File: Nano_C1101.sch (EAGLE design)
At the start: 7 parts

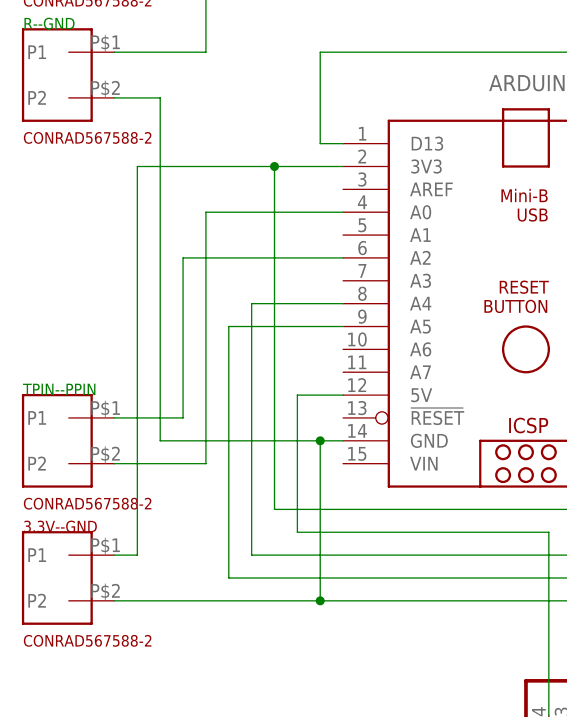
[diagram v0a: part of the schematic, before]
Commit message: few typos, 3V3 -> 5V
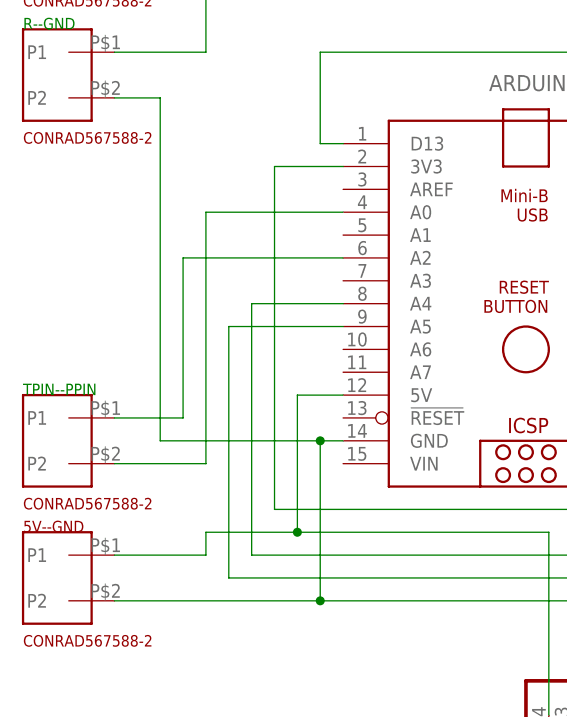
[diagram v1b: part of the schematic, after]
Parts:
- renumbered 3.3V--GND to 5V--GND
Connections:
- net 3V3: no longer 5V--GND.P1
- net 5V: now also 5V--GND.P1
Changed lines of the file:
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@@
 </classes>
 <parts>
-<part name="3.3V--GND" library="johannes" deviceset="CONRAD567588-2" device=""/>
+<part name="5V--GND" library="johannes" deviceset="CONRAD567588-2" device=""/>
 <part name="TPIN--PPIN" library="johannes" deviceset="CONRAD567588-2" device=""/>
 <part name="R--GND" library="johannes" deviceset="CONRAD567588-2" device=""/>
@@
 </plain>
 <instances>
-<instance part="3.3V--GND" gate="G$1" x="-15.24" y="38.1" smashed="yes" rot="R270">
+<instance part="5V--GND" gate="G$1" x="-15.24" y="38.1" smashed="yes" rot="R270">
 <attribute name="VALUE" x="-20.32" y="30.48" size="1.27" layer="94"/>
 <attribute name="NAME" x="-20.32" y="43.18" size="1.27" layer="94"/>
@@
 <wire x1="-5.08" y1="53.34" x2="12.7" y2="53.34" width="0.1524" layer="91"/>
 <junction x="12.7" y="53.34"/>
-<pinref part="3.3V--GND" gate="G$1" pin="P2"/>
+<pinref part="5V--GND" gate="G$1" pin="P2"/>
 <wire x1="-10.16" y1="35.56" x2="12.7" y2="35.56" width="0.1524" layer="91"/>
 <junction x="12.7" y="35.56"/>
@@
 <wire x1="73.66" y1="55.88" x2="86.36" y2="55.88" width="0.1524" layer="91"/>
 <wire x1="7.62" y1="45.72" x2="7.62" y2="83.82" width="0.1524" layer="91"/>
-<wire x1="-7.62" y1="83.82" x2="-7.62" y2="40.64" width="0.1524" layer="91"/>
-<pinref part="3.3V--GND" gate="G$1" pin="P1"/>
-<wire x1="-7.62" y1="40.64" x2="-10.16" y2="40.64" width="0.1524" layer="91"/>
-<wire x1="-7.62" y1="83.82" x2="7.62" y2="83.82" width="0.1524" layer="91"/>
 <pinref part="ARDUINO_NANO1" gate="G$1" pin="3V3"/>
 <wire x1="7.62" y1="83.82" x2="15.24" y2="83.82" width="0.1524" layer="91"/>
-<junction x="7.62" y="83.82"/>
 </segment>
 </net>
@@
 <pinref part="OLED" gate="A" pin="4"/>
 <wire x1="38.1" y1="43.18" x2="38.1" y2="22.86" width="0.1524" layer="91"/>
+<pinref part="5V--GND" gate="G$1" pin="P1"/>
+<wire x1="-10.16" y1="40.64" x2="0" y2="40.64" width="0.1524" layer="91"/>
+<wire x1="0" y1="40.64" x2="0" y2="43.18" width="0.1524" layer="91"/>
+<wire x1="0" y1="43.18" x2="10.16" y2="43.18" width="0.1524" layer="91"/>
+<junction x="10.16" y="43.18"/>
 </segment>
 </net>
@@
 </sheet>
 </sheets>
+<errors>
+</errors>
 </schematic>
 </drawing>

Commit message: Semi-final version of Nano_C1101
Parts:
- added JP1: (no value), adafruit:PINHD-1X1
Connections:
- new net N$1: ARDUINO_NANO1.D6, JP1.1
- net G-RGB: now also ARDUINO_NANO1.D7; no longer ARDUINO_NANO1.D6
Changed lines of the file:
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@@
 <layer number="54" name="bGND_GNDA" color="1" fill="9" visible="no" active="no"/>
 <layer number="56" name="wert" color="7" fill="1" visible="no" active="no"/>
+<layer number="57" name="tCAD" color="7" fill="1" visible="no" active="no"/>
+<layer number="59" name="tCarbon" color="7" fill="1" visible="no" active="no"/>
+<layer number="60" name="bCarbon" color="7" fill="1" visible="no" active="no"/>
 <layer number="88" name="SimResults" color="9" fill="1" visible="yes" active="yes"/>
 <layer number="89" name="SimProbes" color="9" fill="1" visible="yes" active="yes"/>
@@
 <layer number="97" name="Info" color="7" fill="1" visible="yes" active="yes"/>
 <layer number="98" name="Guide" color="6" fill="1" visible="yes" active="yes"/>
+<layer number="99" name="SpiceOrder" color="7" fill="1" visible="no" active="no"/>
 <layer number="100" name="Muster" color="7" fill="1" visible="no" active="no"/>
 <layer number="101" name="Patch_Top" color="12" fill="4" visible="yes" active="yes"/>
@@
 <layer number="106" name="bPlate" color="7" fill="1" visible="yes" active="yes"/>
 <layer number="107" name="Crop" color="7" fill="1" visible="yes" active="yes"/>
+<layer number="108" name="fp8" color="7" fill="1" visible="no" active="yes"/>
+<layer number="109" name="fp9" color="7" fill="1" visible="no" active="yes"/>
+<layer number="110" name="fp0" color="7" fill="1" visible="no" active="yes"/>
+<layer number="111" name="LPC17xx" color="7" fill="1" visible="no" active="yes"/>
+<layer number="112" name="tSilk" color="7" fill="1" visible="no" active="yes"/>
+<layer number="113" name="ReferenceLS" color="7" fill="1" visible="no" active="no"/>
 <layer number="116" name="Patch_BOT" color="9" fill="4" visible="yes" active="yes"/>
+<layer number="118" name="Rect_Pads" color="7" fill="1" visible="no" active="no"/>
 <layer number="121" name="_tsilk" color="7" fill="1" visible="yes" active="yes"/>
 <layer number="122" name="_bsilk" color="7" fill="1" visible="yes" active="yes"/>
+<layer number="123" name="tTestmark" color="7" fill="1" visible="no" active="yes"/>
+<layer number="124" name="bTestmark" color="7" fill="1" visible="no" active="yes"/>
 <layer number="125" name="_tNames" color="7" fill="1" visible="yes" active="yes"/>
+<layer number="126" name="_bNames" color="7" fill="1" visible="no" active="yes"/>
+<layer number="127" name="_tValues" color="7" fill="1" visible="no" active="yes"/>
+<layer number="128" name="_bValues" color="7" fill="1" visible="no" active="yes"/>
+<layer number="129" name="Mask" color="7" fill="1" visible="yes" active="yes"/>
+<layer number="131" name="tAdjust" color="7" fill="1" visible="no" active="yes"/>
+<layer number="132" name="bAdjust" color="7" fill="1" visible="no" active="yes"/>
 <layer number="144" name="Drill_legend" color="7" fill="1" visible="yes" active="yes"/>
+<layer number="150" name="Notes" color="7" fill="1" visible="no" active="yes"/>
 <layer number="151" name="HeatSink" color="7" fill="1" visible="yes" active="yes"/>
+<layer number="152" name="_bDocu" color="7" fill="1" visible="no" active="yes"/>
+<layer number="153" name="FabDoc1" color="6" fill="1" visible="no" active="no"/>
+<layer number="154" name="FabDoc2" color="2" fill="1" visible="no" active="no"/>
+<layer number="155" name="FabDoc3" color="7" fill="15" visible="no" active="no"/>
+<layer number="199" name="Contour" color="7" fill="1" visible="no" active="yes"/>
 <layer number="200" name="200bmp" color="1" fill="10" visible="yes" active="yes"/>
 <layer number="201" name="201bmp" color="2" fill="10" visible="yes" active="yes"/>
@@
 <layer number="223" name="223bmp" color="24" fill="1" visible="no" active="no"/>
 <layer number="224" name="224bmp" color="25" fill="1" visible="no" active="no"/>
+<layer number="225" name="225bmp" color="7" fill="1" visible="yes" active="yes"/>
+<layer number="226" name="226bmp" color="7" fill="1" visible="yes" active="yes"/>
+<layer number="227" name="227bmp" color="7" fill="1" visible="yes" active="yes"/>
+<layer number="228" name="228bmp" color="7" fill="1" visible="yes" active="yes"/>
+<layer number="229" name="229bmp" color="7" fill="1" visible="yes" active="yes"/>
+<layer number="230" name="230bmp" color="7" fill="1" visible="yes" active="yes"/>
+<layer number="231" name="Eagle3D_PG1" color="7" fill="1" visible="no" active="no"/>
+<layer number="232" name="Eagle3D_PG2" color="7" fill="1" visible="no" active="no"/>
+<layer number="233" name="Eagle3D_PG3" color="7" fill="1" visible="no" active="no"/>
+<layer number="248" name="Housing" color="7" fill="1" visible="no" active="yes"/>
+<layer number="249" name="Edge" color="7" fill="1" visible="no" active="yes"/>
 <layer number="250" name="Descript" color="3" fill="1" visible="no" active="no"/>
 <layer number="251" name="SMDround" color="12" fill="11" visible="no" active="no"/>
 <layer number="254" name="cooling" color="7" fill="1" visible="yes" active="yes"/>
+<layer number="255" name="routoute" color="7" fill="1" visible="yes" active="yes"/>
 </layers>
 <schematic xreflabel="%F%N/%S.%C%R" xrefpart="/%S.%C%R">
@@
 <part name="U$1" library="johannes" deviceset="NEUFTECH_CC1101" device=""/>
 <part name="OLED" library="pinhead" library_urn="urn:adsk.eagle:library:325" deviceset="PINHD-1X4" device="" package3d_urn="urn:adsk.eagle:package:22407/2"/>
+<part name="JP1" library="adafruit" library_urn="urn:adsk.eagle:library:420" deviceset="PINHD-1X1" device="" package3d_urn="urn:adsk.eagle:package:6240654/1"/>
 </parts>
 <sheets>
@@
 <attribute name="NAME" x="48.895" y="26.67" size="1.778" layer="95" rot="R270"/>
 <attribute name="VALUE" x="33.02" y="26.67" size="1.778" layer="96" rot="R270"/>
+</instance>
+<instance part="JP1" gate="G$1" x="-15.24" y="73.66" smashed="yes">
+<attribute name="NAME" x="-21.59" y="76.835" size="1.778" layer="95"/>
+<attribute name="VALUE" x="-21.59" y="68.58" size="1.778" layer="96"/>
 </instance>
 </instances>
@@
 <segment>
 <pinref part="G--B" gate="G$1" pin="P1"/>
-<wire x1="-10.16" y1="111.76" x2="76.2" y2="111.76" width="0.1524" layer="91"/>
-<wire x1="76.2" y1="111.76" x2="76.2" y2="71.12" width="0.1524" layer="91"/>
-<wire x1="76.2" y1="71.12" x2="55.88" y2="71.12" width="0.1524" layer="91"/>
-<pinref part="ARDUINO_NANO1" gate="G$1" pin="D6"/>
+<wire x1="-10.16" y1="111.76" x2="71.12" y2="111.76" width="0.1524" layer="91"/>
+<pinref part="ARDUINO_NANO1" gate="G$1" pin="D7"/>
+<wire x1="55.88" y1="73.66" x2="76.2" y2="73.66" width="0.1524" layer="91"/>
+<wire x1="76.2" y1="73.66" x2="76.2" y2="111.76" width="0.1524" layer="91"/>
+<wire x1="76.2" y1="111.76" x2="71.12" y2="111.76" width="0.1524" layer="91"/>
 </segment>
 </net>
@@
 </segment>
 </net>
+<net name="N$1" class="0">
+<segment>
+<pinref part="ARDUINO_NANO1" gate="G$1" pin="D6"/>
+<wire x1="55.88" y1="71.12" x2="68.58" y2="71.12" width="0.1524" layer="91"/>
+<wire x1="68.58" y1="71.12" x2="68.58" y2="104.14" width="0.1524" layer="91"/>
+<wire x1="68.58" y1="104.14" x2="2.54" y2="104.14" width="0.1524" layer="91"/>
+<wire x1="2.54" y1="104.14" x2="2.54" y2="81.28" width="0.1524" layer="91"/>
+<wire x1="2.54" y1="81.28" x2="-10.16" y2="81.28" width="0.1524" layer="91"/>
+<wire x1="-10.16" y1="81.28" x2="-10.16" y2="73.66" width="0.1524" layer="91"/>
+<wire x1="-10.16" y1="73.66" x2="-17.78" y2="73.66" width="0.1524" layer="91"/>
+<pinref part="JP1" gate="G$1" pin="1"/>
+</segment>
+</net>

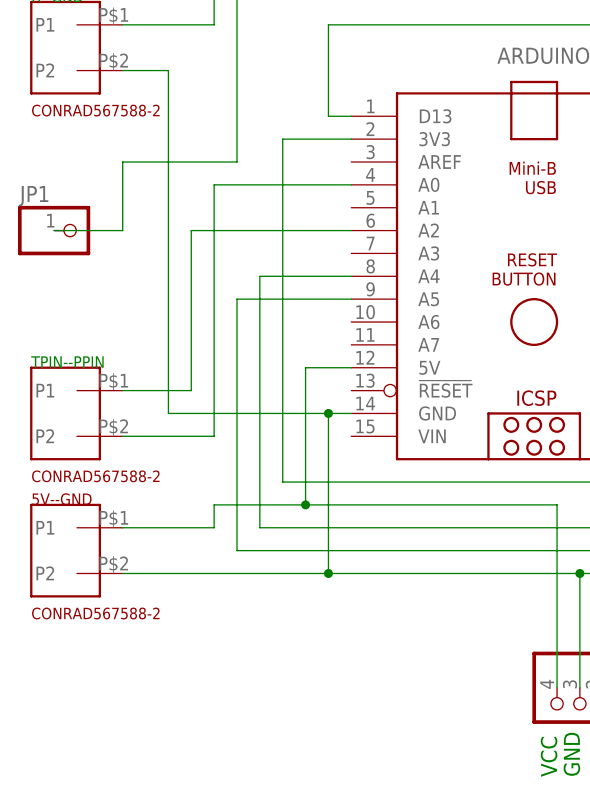
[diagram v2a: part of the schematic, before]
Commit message: Added resistor and more pins for sensors
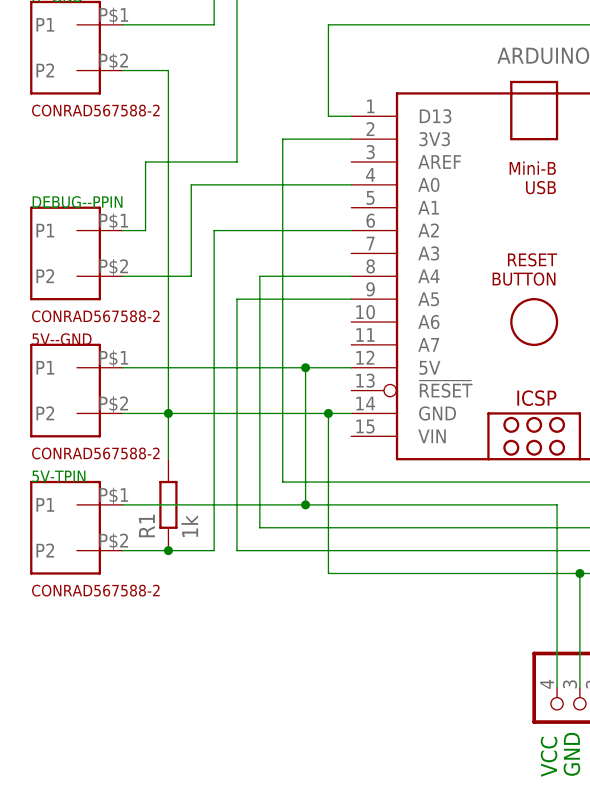
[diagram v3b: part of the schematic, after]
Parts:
- removed JP1: (no value), adafruit:PINHD-1X1
- removed TPIN--PPIN: CONRAD567588-2, johannes:CONRAD567588-2
- added 5V-TPIN, DEBUG--PPIN: CONRAD567588-2, johannes:CONRAD567588-2
- added R1: 1k, rcl:R-EU_0204/7
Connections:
- removed net N$1: ARDUINO_NANO1.D6, JP1.1
- new net DEBUG: ARDUINO_NANO1.D6, DEBUG--PPIN.P1
- net 5V: now also 5V-TPIN.P1
- net GND: now also R1.2
- net PPIN: now also DEBUG--PPIN.P2; no longer TPIN--PPIN.P2
- net TPIN: now also 5V-TPIN.P2, R1.1; no longer TPIN--PPIN.P1
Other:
- moved on the sheet: 5V--GND
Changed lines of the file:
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@@
 <parts>
 <part name="5V--GND" library="johannes" deviceset="CONRAD567588-2" device=""/>
-<part name="TPIN--PPIN" library="johannes" deviceset="CONRAD567588-2" device=""/>
+<part name="DEBUG--PPIN" library="johannes" deviceset="CONRAD567588-2" device=""/>
 <part name="R--GND" library="johannes" deviceset="CONRAD567588-2" device=""/>
 <part name="G--B" library="johannes" deviceset="CONRAD567588-2" device=""/>
@@
 <part name="U$1" library="johannes" deviceset="NEUFTECH_CC1101" device=""/>
 <part name="OLED" library="pinhead" library_urn="urn:adsk.eagle:library:325" deviceset="PINHD-1X4" device="" package3d_urn="urn:adsk.eagle:package:22407/2"/>
-<part name="JP1" library="adafruit" library_urn="urn:adsk.eagle:library:420" deviceset="PINHD-1X1" device="" package3d_urn="urn:adsk.eagle:package:6240654/1"/>
+<part name="R1" library="rcl" library_urn="urn:adsk.eagle:library:334" deviceset="R-EU_" device="0204/7" package3d_urn="urn:adsk.eagle:package:23498/2" value="1k"/>
+<part name="5V-TPIN" library="johannes" deviceset="CONRAD567588-2" device=""/>
 </parts>
 <sheets>
@@
 </plain>
 <instances>
-<instance part="5V--GND" gate="G$1" x="-15.24" y="38.1" smashed="yes" rot="R270">
-<attribute name="VALUE" x="-20.32" y="30.48" size="1.27" layer="94"/>
-<attribute name="NAME" x="-20.32" y="43.18" size="1.27" layer="94"/>
-</instance>
-<instance part="TPIN--PPIN" gate="G$1" x="-15.24" y="53.34" smashed="yes" rot="R270">
-<attribute name="VALUE" x="-20.32" y="45.72" size="1.27" layer="94"/>
-<attribute name="NAME" x="-20.32" y="58.42" size="1.27" layer="91"/>
+<instance part="5V--GND" gate="G$1" x="-15.24" y="55.88" smashed="yes" rot="R270">
+<attribute name="VALUE" x="-20.32" y="48.26" size="1.27" layer="94"/>
+<attribute name="NAME" x="-20.32" y="60.96" size="1.27" layer="94"/>
+</instance>
+<instance part="DEBUG--PPIN" gate="G$1" x="-15.24" y="71.12" smashed="yes" rot="R270">
+<attribute name="VALUE" x="-20.32" y="63.5" size="1.27" layer="94"/>
+<attribute name="NAME" x="-20.32" y="76.2" size="1.27" layer="91"/>
 </instance>
 <instance part="R--GND" gate="G$1" x="-15.24" y="93.98" smashed="yes" rot="R270">
@@
 <attribute name="VALUE" x="33.02" y="26.67" size="1.778" layer="96" rot="R270"/>
 </instance>
-<instance part="JP1" gate="G$1" x="-15.24" y="73.66" smashed="yes">
-<attribute name="NAME" x="-21.59" y="76.835" size="1.778" layer="95"/>
-<attribute name="VALUE" x="-21.59" y="68.58" size="1.778" layer="96"/>
+<instance part="R1" gate="G$1" x="-5.08" y="43.18" smashed="yes" rot="R90">
+<attribute name="NAME" x="-6.5786" y="39.37" size="1.778" layer="95" rot="R90"/>
+<attribute name="VALUE" x="-1.778" y="39.37" size="1.778" layer="96" rot="R90"/>
+</instance>
+<instance part="5V-TPIN" gate="G$1" x="-15.24" y="40.64" smashed="yes" rot="R270">
+<attribute name="VALUE" x="-20.32" y="33.02" size="1.27" layer="94"/>
+<attribute name="NAME" x="-20.32" y="45.72" size="1.27" layer="91"/>
 </instance>
 </instances>
@@
 </busses>
 <nets>
-<net name="TPIN" class="0">
-<segment>
-<wire x1="-2.54" y1="55.88" x2="-2.54" y2="73.66" width="0.1524" layer="91"/>
-<wire x1="-2.54" y1="73.66" x2="15.24" y2="73.66" width="0.1524" layer="91"/>
-<pinref part="ARDUINO_NANO1" gate="G$1" pin="A2"/>
-<pinref part="TPIN--PPIN" gate="G$1" pin="P1"/>
-<wire x1="-2.54" y1="55.88" x2="-10.16" y2="55.88" width="0.1524" layer="91"/>
-</segment>
-</net>
 <net name="PPIN" class="0">
 <segment>
-<wire x1="0" y1="50.8" x2="0" y2="78.74" width="0.1524" layer="91"/>
-<wire x1="0" y1="78.74" x2="15.24" y2="78.74" width="0.1524" layer="91"/>
+<wire x1="-2.54" y1="68.58" x2="-2.54" y2="78.74" width="0.1524" layer="91"/>
+<wire x1="-2.54" y1="78.74" x2="15.24" y2="78.74" width="0.1524" layer="91"/>
 <pinref part="ARDUINO_NANO1" gate="G$1" pin="A0"/>
-<pinref part="TPIN--PPIN" gate="G$1" pin="P2"/>
-<wire x1="0" y1="50.8" x2="-10.16" y2="50.8" width="0.1524" layer="91"/>
+<pinref part="DEBUG--PPIN" gate="G$1" pin="P2"/>
+<wire x1="-2.54" y1="68.58" x2="-10.16" y2="68.58" width="0.1524" layer="91"/>
 </segment>
 </net>
@@
 <wire x1="40.64" y1="35.56" x2="12.7" y2="35.56" width="0.1524" layer="91"/>
 <wire x1="12.7" y1="35.56" x2="12.7" y2="53.34" width="0.1524" layer="91"/>
-<pinref part="R--GND" gate="G$1" pin="P2"/>
-<wire x1="-10.16" y1="91.44" x2="-5.08" y2="91.44" width="0.1524" layer="91"/>
-<wire x1="-5.08" y1="91.44" x2="-5.08" y2="53.34" width="0.1524" layer="91"/>
-<wire x1="-5.08" y1="53.34" x2="12.7" y2="53.34" width="0.1524" layer="91"/>
-<junction x="12.7" y="53.34"/>
-<pinref part="5V--GND" gate="G$1" pin="P2"/>
-<wire x1="-10.16" y1="35.56" x2="12.7" y2="35.56" width="0.1524" layer="91"/>
-<junction x="12.7" y="35.56"/>
 <pinref part="OLED" gate="A" pin="3"/>
 <wire x1="40.64" y1="22.86" x2="40.64" y2="35.56" width="0.1524" layer="91"/>
 <junction x="40.64" y="35.56"/>
+<pinref part="5V--GND" gate="G$1" pin="P2"/>
+<wire x1="-10.16" y1="53.34" x2="-5.08" y2="53.34" width="0.1524" layer="91"/>
+<junction x="12.7" y="53.34"/>
+<pinref part="R--GND" gate="G$1" pin="P2"/>
+<wire x1="-5.08" y1="53.34" x2="12.7" y2="53.34" width="0.1524" layer="91"/>
+<wire x1="-10.16" y1="91.44" x2="-5.08" y2="91.44" width="0.1524" layer="91"/>
+<wire x1="-5.08" y1="91.44" x2="-5.08" y2="53.34" width="0.1524" layer="91"/>
+<pinref part="R1" gate="G$1" pin="2"/>
+<junction x="-5.08" y="53.34"/>
+<wire x1="-5.08" y1="53.34" x2="-5.08" y2="48.26" width="0.1524" layer="91"/>
 </segment>
 </net>
@@
 <segment>
 <pinref part="ARDUINO_NANO1" gate="G$1" pin="5V"/>
-<wire x1="15.24" y1="58.42" x2="10.16" y2="58.42" width="0.1524" layer="91"/>
-<wire x1="10.16" y1="58.42" x2="10.16" y2="43.18" width="0.1524" layer="91"/>
 <wire x1="10.16" y1="43.18" x2="38.1" y2="43.18" width="0.1524" layer="91"/>
 <pinref part="OLED" gate="A" pin="4"/>
 <wire x1="38.1" y1="43.18" x2="38.1" y2="22.86" width="0.1524" layer="91"/>
 <pinref part="5V--GND" gate="G$1" pin="P1"/>
-<wire x1="-10.16" y1="40.64" x2="0" y2="40.64" width="0.1524" layer="91"/>
-<wire x1="0" y1="40.64" x2="0" y2="43.18" width="0.1524" layer="91"/>
-<wire x1="0" y1="43.18" x2="10.16" y2="43.18" width="0.1524" layer="91"/>
+<wire x1="-10.16" y1="58.42" x2="10.16" y2="58.42" width="0.1524" layer="91"/>
+<wire x1="10.16" y1="58.42" x2="10.16" y2="43.18" width="0.1524" layer="91"/>
+<wire x1="10.16" y1="58.42" x2="15.24" y2="58.42" width="0.1524" layer="91"/>
+<junction x="10.16" y="58.42"/>
+<pinref part="5V-TPIN" gate="G$1" pin="P1"/>
+<wire x1="-10.16" y1="43.18" x2="10.16" y2="43.18" width="0.1524" layer="91"/>
 <junction x="10.16" y="43.18"/>
 </segment>
 </net>
-<net name="N$1" class="0">
+<net name="DEBUG" class="0">
 <segment>
 <pinref part="ARDUINO_NANO1" gate="G$1" pin="D6"/>
@@
 <wire x1="68.58" y1="104.14" x2="2.54" y2="104.14" width="0.1524" layer="91"/>
 <wire x1="2.54" y1="104.14" x2="2.54" y2="81.28" width="0.1524" layer="91"/>
-<wire x1="2.54" y1="81.28" x2="-10.16" y2="81.28" width="0.1524" layer="91"/>
-<wire x1="-10.16" y1="81.28" x2="-10.16" y2="73.66" width="0.1524" layer="91"/>
-<wire x1="-10.16" y1="73.66" x2="-17.78" y2="73.66" width="0.1524" layer="91"/>
-<pinref part="JP1" gate="G$1" pin="1"/>
+<wire x1="2.54" y1="81.28" x2="-7.62" y2="81.28" width="0.1524" layer="91"/>
+<wire x1="-7.62" y1="81.28" x2="-7.62" y2="73.66" width="0.1524" layer="91"/>
+<pinref part="DEBUG--PPIN" gate="G$1" pin="P1"/>
+<wire x1="-7.62" y1="73.66" x2="-10.16" y2="73.66" width="0.1524" layer="91"/>
+</segment>
+</net>
+<net name="TPIN" class="0">
+<segment>
+<pinref part="5V-TPIN" gate="G$1" pin="P2"/>
+<wire x1="-10.16" y1="38.1" x2="-5.08" y2="38.1" width="0.1524" layer="91"/>
+<wire x1="-5.08" y1="38.1" x2="0" y2="38.1" width="0.1524" layer="91"/>
+<wire x1="0" y1="38.1" x2="0" y2="73.66" width="0.1524" layer="91"/>
+<pinref part="R1" gate="G$1" pin="1"/>
+<junction x="-5.08" y="38.1"/>
+<pinref part="ARDUINO_NANO1" gate="G$1" pin="A2"/>
+<wire x1="15.24" y1="73.66" x2="0" y2="73.66" width="0.1524" layer="91"/>
 </segment>
 </net>
@@
 packages will not be understood (or retained) with this version.
 </note>
+<note version="8.4" severity="warning">
+Since Version 8.4, EAGLE supports properties for SPICE simulation.
+Probes in schematics and SPICE mapping objects found in parts and library devices
+will not be understood with this version. Update EAGLE to the latest version
+for full support of SPICE simulation.
+</note>
 </compatibility>
